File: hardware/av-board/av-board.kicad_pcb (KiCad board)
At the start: 4 copper layers, 94.6 x 69.4 mm, 222 parts, among them J1 RCA Y, J10 2x20 socket, J2 RCA Pb, J3 RCA Pr, J4 RCA L, J5 RCA R, J6 HDMI-001, J9 2x20 socket, SW1 TS-1187A-B-A-B, SW2 TS-1187A-B-A-B, U1 ADV7842KBCZ-5, U10 TPD4E05U06DQAR, U2 ADV7511KSTZ, U3 PCM1808PWR, U4 TLV62569DBVR, U5 TPS7A7001DDAR, U6 TPS7A7001DDAR, U7 TPS7A7001DDAR, U8 TPD4E05U06DQAR, U9 TPD4E05U06DQAR, Y1 28.63636MHz 20pF

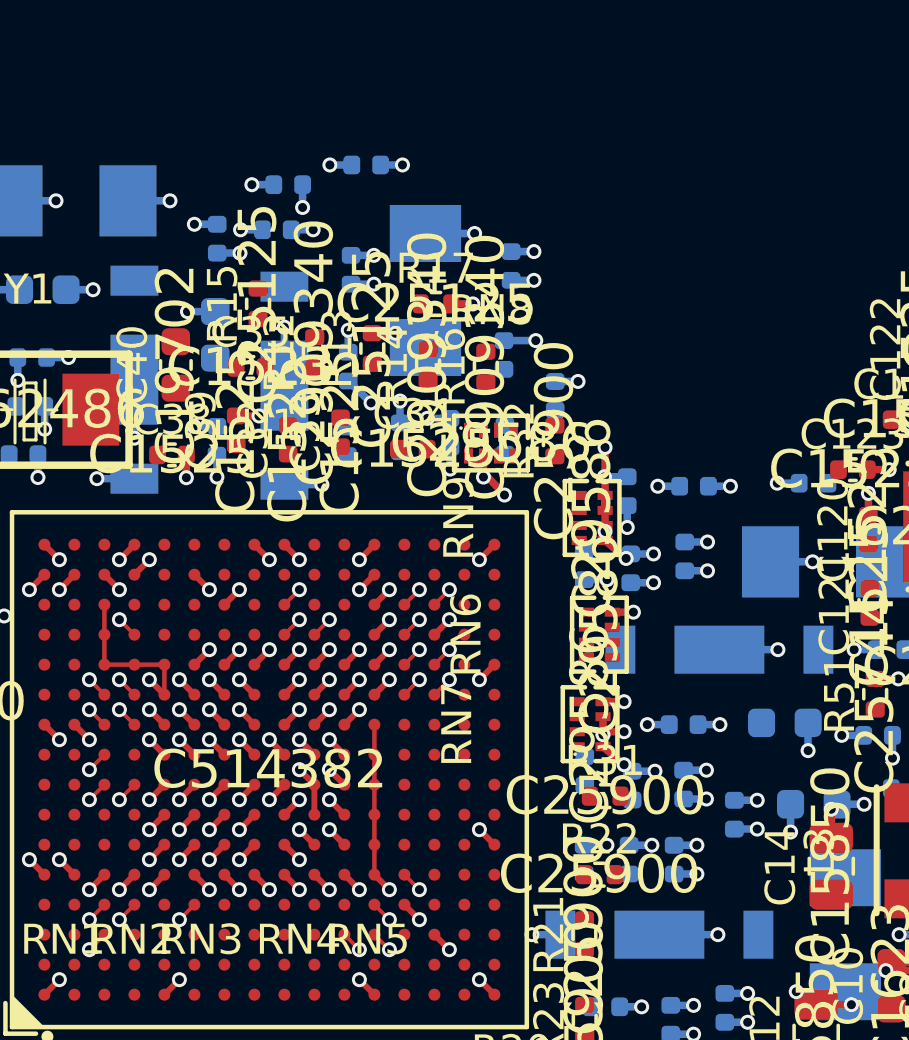
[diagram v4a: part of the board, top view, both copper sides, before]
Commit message: SDRAM pull-downs grouped by ball position, arrays along the BGA's right side; six layers default
The pull-down arrays were grouped by DQ number, so each collected four lines from scattered
balls across the BGA's top right corner (RN8: R16, R15, T15 and N14, four rows in), and lines
for different arrays crossed in the tightest spot on the board. Any pin may take any of these
identical 4.7 k pull-downs, so:

- board.py orders the 18 balls along the chip's T-row edge (column, then row); each array serves
  four neighbouring balls, the two at the ends of the run take single resistors.
- gen_pcb.py's array placer (was place_rn, for the 75 R arrays) takes any side: the pull-down
  arrays now stand in a column down the ADV7842's right side, each level with its balls, pads
  towards the chip in ball order.
- Six layers are the default (LAYERS=4 does not route); design.md says why, with the results.

ERC clean, schematic = board.py (903 pins), DRC: only the unrouted connections.

Co-Authored-By: Claude Opus 5.5 <noreply@anthropic.com>
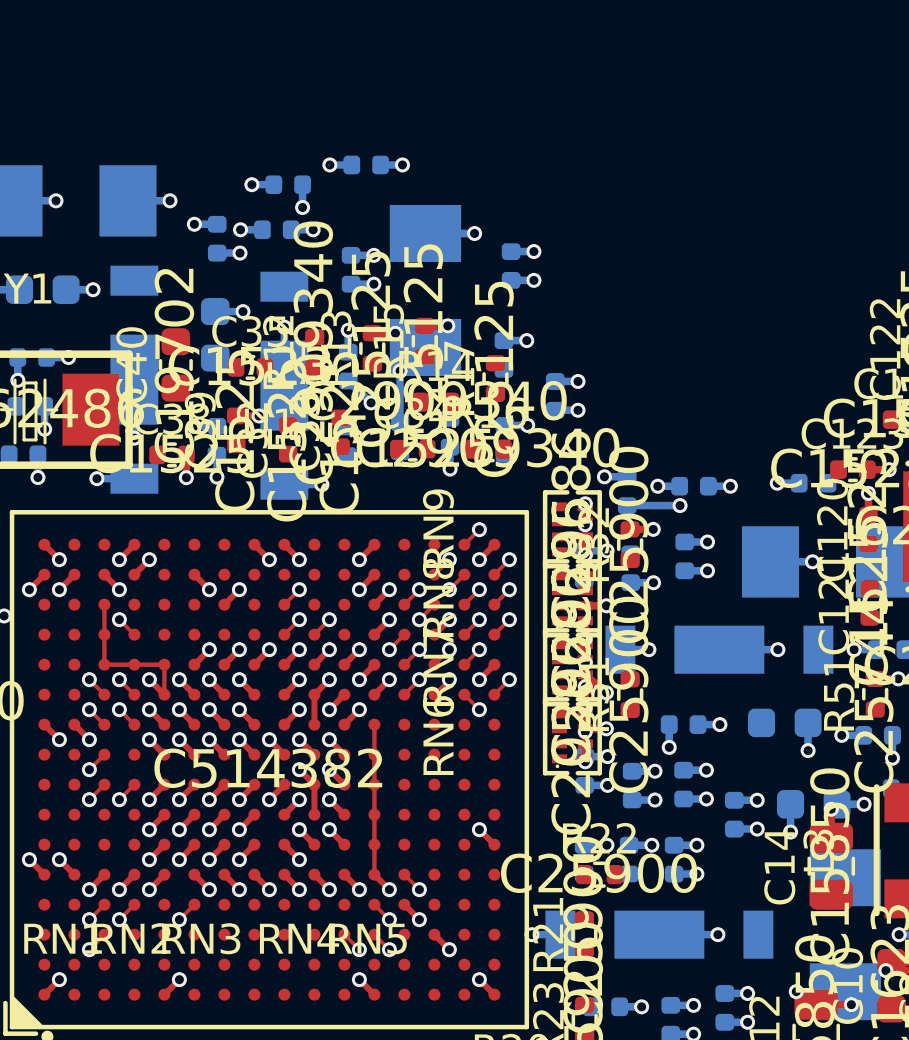
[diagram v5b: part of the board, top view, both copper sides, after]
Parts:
- moved RN8 5.84 mm to (123.1, 55.3), turned to 90 degrees
- moved R15 5.69 mm to (118.2, 46.7)
- moved R32 4.27 mm to (125.0, 53.5)
- moved RN6 3.51 mm to (123.1, 59.9)
- moved R31 3.48 mm to (125.0, 58.5), turned to 90 degrees
- moved R17 3.18 mm to (120.5, 48.0), turned to 90 degrees
- moved R16 2.74 mm to (120.3, 50.3), turned to 0 degrees
- moved RN7 1.99 mm to (123.1, 57.6)
- moved R14 1.28 mm to (118.5, 48.7), turned to 0 degrees
- moved RN9 0.76 mm to (123.1, 53.0)
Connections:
- R32 pad 1: PD_SDRAM_UDQS -> PD_SDRAM_DQ8
- RN6 pad 1: PD_SDRAM_DQ0 -> PD_SDRAM_DQ7
- RN6 pad 2: PD_SDRAM_DQ1 -> PD_SDRAM_DQ6
- RN6 pad 3: PD_SDRAM_DQ2 -> PD_SDRAM_DQ5
- RN6 pad 4: PD_SDRAM_DQ3 -> PD_SDRAM_DQ4
- RN7 pad 1: PD_SDRAM_DQ4 -> PD_SDRAM_DQ3
- RN7 pad 2: PD_SDRAM_DQ5 -> PD_SDRAM_DQ2
- RN7 pad 3: PD_SDRAM_DQ6 -> PD_SDRAM_DQ15
- RN7 pad 4: PD_SDRAM_DQ7 -> PD_SDRAM_DQ0
- RN8 pad 1: PD_SDRAM_DQ8 -> PD_SDRAM_DQ1
- RN8 pad 2: PD_SDRAM_DQ9 -> PD_SDRAM_DQ11
- RN8 pad 3: PD_SDRAM_DQ10 -> PD_SDRAM_DQ12
- RN8 pad 4: PD_SDRAM_DQ11 -> PD_SDRAM_DQ13
- RN9 pad 1: PD_SDRAM_DQ12 -> PD_SDRAM_DQ14
- RN9 pad 2: PD_SDRAM_DQ13 -> PD_SDRAM_UDQS
- RN9 pad 3: PD_SDRAM_DQ14 -> PD_SDRAM_DQ9
- RN9 pad 4: PD_SDRAM_DQ15 -> PD_SDRAM_DQ10
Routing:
- net AV_DVDDIO: track 20.8 -> 22.3 mm, vias 21 -> 23
- net AV_VDD: track 11.9 -> 13.1 mm
- net AV_AVDD: track 14.1 -> 14.9 mm, vias 17 -> 18
- net PD_SDRAM_UDQS: track 0.00 -> 0.71 mm, vias 0 -> 1
- net PD_SDRAM_DQ9: track 0.00 -> 0.71 mm, vias 0 -> 1
- net PD_SDRAM_DQ8: track 0.00 -> 0.71 mm, vias 0 -> 1
- net PD_SDRAM_DQ6: track 0.00 -> 0.71 mm, vias 0 -> 1
- net PD_SDRAM_DQ5: track 0.00 -> 0.71 mm, vias 0 -> 1
- net PD_SDRAM_DQ2: track 0.00 -> 0.71 mm, vias 0 -> 1
- net PD_SDRAM_DQ14: track 0.00 -> 0.71 mm, vias 0 -> 1
- net PD_SDRAM_DQ13: track 0.00 -> 0.71 mm, vias 0 -> 1
- net PD_SDRAM_DQ10: track 0.00 -> 0.71 mm, vias 0 -> 1
- net PD_SDRAM_DQ1: track 0.00 -> 0.71 mm, vias 0 -> 1
- net PD_SDRAM_DQ0: track 0.00 -> 0.71 mm, vias 0 -> 1
- net GND: track 249.6 -> 249.8 mm, vias 270 -> 273
- added copper zone on In3.Cu, net AV_AVDD
- added copper zone on In3.Cu, net AV_DVDDIO
- added copper zone on In3.Cu, net AV_PVDD
- added copper zone on In3.Cu, net AV_TVDD
- added copper zone on In3.Cu, net AV_VDD
- added copper zone on In4.Cu, net GND
- removed copper zone on In2.Cu, net AV_AVDD
- removed copper zone on In2.Cu, net AV_DVDDIO
- removed copper zone on In2.Cu, net AV_PVDD
- removed copper zone on In2.Cu, net AV_TVDD
- removed copper zone on In2.Cu, net AV_VDD
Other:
- copper layers 4 -> 6

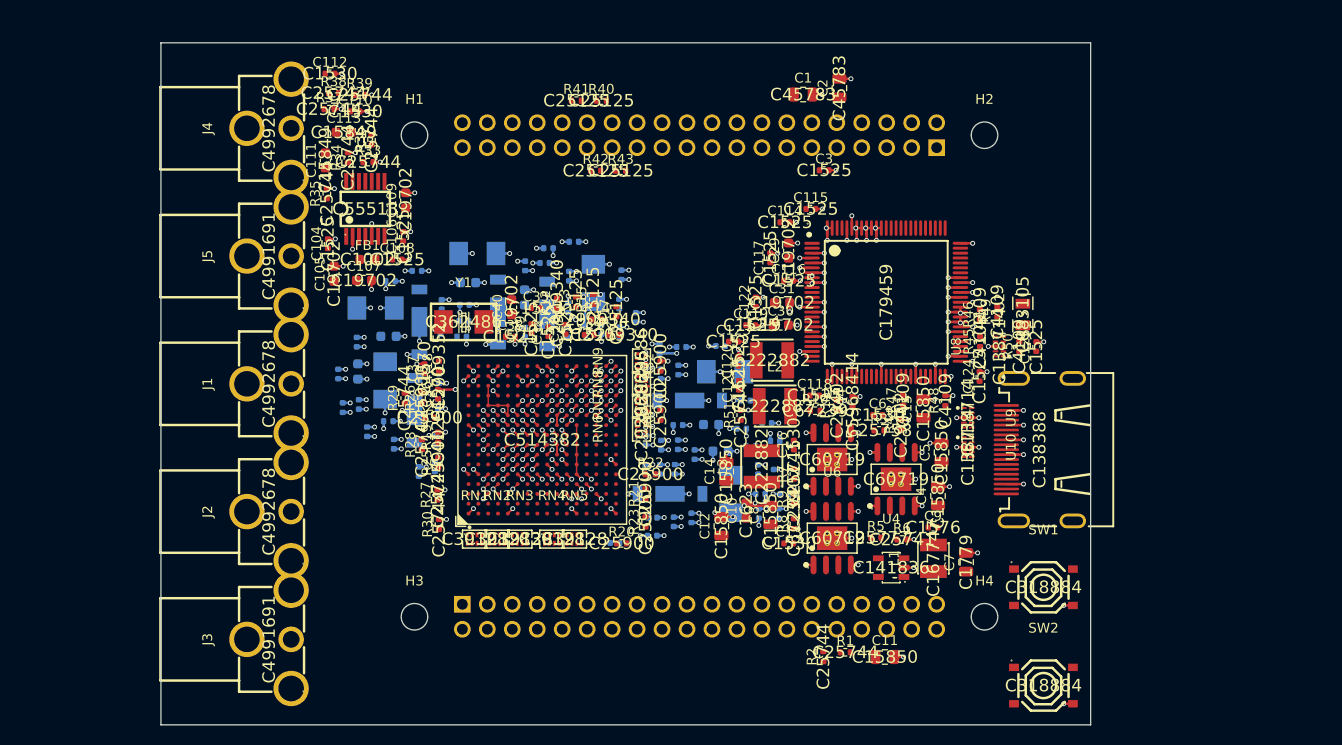
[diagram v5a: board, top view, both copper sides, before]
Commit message: Single pull-down resistors, SYNC_Y escape via, rail caps by their rail pad
From a round of free Freerouting trials (each variant routed on fpga, DRC'd, failures counted
over several runs):

- The unused SDRAM port's 18 pull-downs are single 0402s by the ADV7842's right side. With
  4-resistor arrays two to five of them failed in every run on both routers (four lines meeting a
  0.5 mm-pitch array in order, in the board's tightest corner); with singles, rarely one.
- SYNC_Y (J15) takes an escape via like the pull-down balls: it failed in nearly every run on
  F.Cu under the analog inputs' terminations, and not once with the via.
- A rail cap is placed where its rail pad (0.3 mm in) is over its plane, not its whole footprint:
  all 69 now sit on their planes (three were off). The plane fanout puts a rail pad's via only
  where the via itself lands on the plane (one off it connected nothing), tries 16 directions up
  to 2.5 mm, and names the pads left without one (their caps are joined by a routed track).
- CVDD's filter FL3 sits beside FL6, a short branch off FL4's 1V8A.

Tried and dropped: a wider free ring above the analog edge, more room round each rail cap,
reserved via spots, pull-down arrays on B.Cu or further out, vias for REFP/REFN, turning U5/U7.

Freerouting on this board leaves 2-7 short connections depending on the run. ERC clean,
schematic = board.py, DRC: only the unrouted connections.

Co-Authored-By: Claude Opus 5.5 <noreply@anthropic.com>
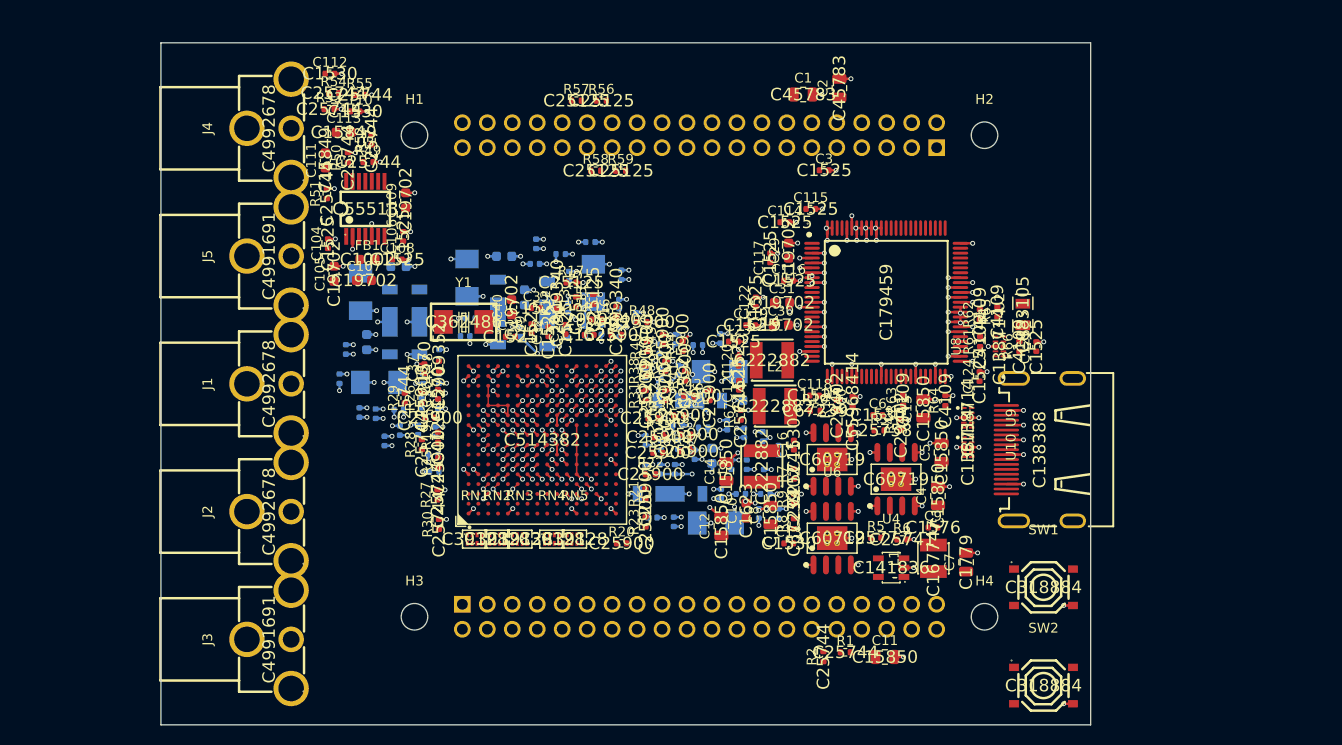
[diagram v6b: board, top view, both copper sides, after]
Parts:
- removed RN6, RN7, RN8, RN9: 4.7k, lcsc:RES-ARRAY-SMD_0402-8P-L2.0-W1.0-BL
- added R52: 10k, Resistor_SMD:R_0402_1005Metric, F.Cu at (95.6, 30.5)
- added R53: 10k, Resistor_SMD:R_0402_1005Metric, F.Cu at (91.3, 27.3)
- added R54: 10k, Resistor_SMD:R_0402_1005Metric, F.Cu at (91.8, 25.7)
- added R55: 10k, Resistor_SMD:R_0402_1005Metric, F.Cu at (94.4, 25.9)
- added R56: 51, Resistor_SMD:R_0402_1005Metric, F.Cu at (119.0, 26.5)
- added R57: 51, Resistor_SMD:R_0402_1005Metric, F.Cu at (116.5, 26.5)
- added R58: 51, Resistor_SMD:R_0402_1005Metric, F.Cu at (118.4, 33.6)
- added R59: 51, Resistor_SMD:R_0402_1005Metric, F.Cu at (121.0, 33.6)
- added R60: 887, Resistor_SMD:R_0402_1005Metric, F.Cu at (144.6, 57.1)
- added R61: 2k, Resistor_SMD:R_0402_1005Metric, F.Cu at (157.6, 51.0)
- added R62: 2k, Resistor_SMD:R_0402_1005Metric, F.Cu at (157.5, 48.2)
- added R63: 2k, Resistor_SMD:R_0402_1005Metric, F.Cu at (149.7, 57.0)
- added R64: 2k, Resistor_SMD:R_0402_1005Metric, F.Cu at (154.0, 57.0)
- added R65: 2k, Resistor_SMD:R_0402_1005Metric, F.Cu at (159.3, 48.0)
- added R66: 2k, Resistor_SMD:R_0402_1005Metric, F.Cu at (161.6, 51.5)
- added R67: 10k, Resistor_SMD:R_0402_1005Metric, F.Cu at (133.2, 58.5)
- R33, R34, R35, R36, R37, R38, R39: value 10k -> 4.7k
- R40, R41, R42, R43: value 51 -> 4.7k
- R44: value 887 -> 4.7k
- R45, R46, R47, R48: value 2k -> 4.7k
- R49, R50: value 2k -> 10k
- moved R50 71.0 mm to (93.2, 32.3)
- moved R49 65.8 mm to (95.3, 32.7), turned to 0 degrees
- moved R37 49.1 mm to (127.6, 60.5)
- moved R51 47.8 mm to (91.1, 36.0)
- moved R36 43.1 mm to (124.8, 62.3), turned to 0 degrees
- moved R34 42.7 mm to (126.9, 58.5), turned to 0 degrees
- moved R38 42.5 mm to (123.5, 54.0), turned to 90 degrees
- moved R35 41.9 mm to (124.9, 60.7), turned to 0 degrees
- moved R39 41.6 mm to (125.5, 53.5), turned to 90 degrees
- moved R33 39.0 mm to (124.3, 58.8)
- moved R45 37.0 mm to (120.5, 50.3), turned to 0 degrees
- moved R48 31.9 mm to (123.1, 49.0), turned to 0 degrees
- moved R41 30.1 mm to (127.5, 54.5), turned to 90 degrees
- moved R46 28.7 mm to (130.0, 56.5)
- moved R40 25.4 mm to (123.7, 51.5), turned to 90 degrees
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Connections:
- R31 pad 1: PD_SDRAM_LDQS -> PD_SDRAM_DQ0
- R32 pad 1: PD_SDRAM_DQ8 -> PD_SDRAM_DQ1
- R33 pad 1: MD0 -> PD_SDRAM_DQ2
- R34 pad 1: MD1 -> PD_SDRAM_DQ3
- R35 pad 1: FMT -> PD_SDRAM_DQ4
- R36 pad 1: RCA_L -> PD_SDRAM_DQ5
- R36 pad 2: AUD_DIV_L -> GND
- R37 pad 1: AUD_DIV_L -> PD_SDRAM_DQ6
- R38 pad 1: RCA_R -> PD_SDRAM_DQ7
- R38 pad 2: AUD_DIV_R -> GND
- R39 pad 1: AUD_DIV_R -> PD_SDRAM_DQ8
- R40 pad 1: OUT_MCLK -> PD_SDRAM_DQ9
- R40 pad 2: TX_MCLK -> GND
- R41 pad 1: OUT_SCLK -> PD_SDRAM_DQ10
- R41 pad 2: TX_SCLK -> GND
- R42 pad 1: OUT_LRCLK -> PD_SDRAM_DQ11
- R42 pad 2: TX_LRCLK -> GND
- R43 pad 1: OUT_I2S0 -> PD_SDRAM_DQ12
- R43 pad 2: TX_I2S0 -> GND
- R44 pad 1: R_EXT -> PD_SDRAM_DQ13
- R45 pad 1: 3V3 -> PD_SDRAM_DQ14
- R45 pad 2: OUT_SCL -> GND
- R46 pad 1: 3V3 -> PD_SDRAM_DQ15
- R46 pad 2: OUT_SDA -> GND
- R47 pad 1: 3V3 -> PD_SDRAM_LDQS
- R47 pad 2: OUT_INT -> GND
- R48 pad 1: OUT_PD -> PD_SDRAM_UDQS
- R49 pad 1: HDMI_5V -> MD0
- R49 pad 2: HDMI_SCL -> GND
- R50 pad 1: HDMI_5V -> MD1
- R50 pad 2: HDMI_SDA -> GND
- R51 pad 1: HDMI_HPD -> FMT
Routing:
- net AV_DVDDIO: track 22.3 -> 27.3 mm, vias 23 -> 25
- net AV_VDD: track 13.1 -> 16.8 mm, vias 15 -> 17
- net GND: track 249.8 -> 246.8 mm, vias 273 -> 268
- net AV_TVDD: track 14.7 -> 15.5 mm, vias 18 -> 19
- net SYNC_Y: track 0.00 -> 0.71 mm, vias 0 -> 1
- net AV_AVDD: track 14.9 -> 15.1 mm, vias 18 -> 16

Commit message: The AV board routed: six layers, DRC clean
av-board.kicad_pcb is now routed: Freerouting 1.9 (60 passes) on the six-layer placement, then
mazeroute.py for the two connections it left (C20's AVDD pad round C54, and the Y5 pixel line
from U1 L2 to RN5). DRC: no unconnected items, no clearance or short violations, nothing
dangling; only silkscreen warnings and the two sockets' renumbered pads.

mazeroute.py is a small grid router (A*) for what an autorouter leaves: one net between two
pads on F.Cu/In2.Cu/B.Cu, round everything on the board with our clearances, a new via where
one fits on all layers with drill spacing; obstacles dumped by KiCad's python, the search in
numpy (eda-venv), the result applied back and the zones refilled. Paths start and end at pad
centres.

Checked after routing (design.md "Routing"): nothing switching near R_EXT; TMDS intra-pair skew
at most 2.4 mm, but Freerouting routes the pairs' halves apart, through vias: laying the four
pairs in by hand, coupled and matched, is the next step.

Co-Authored-By: Claude Opus 5.5 <noreply@anthropic.com>
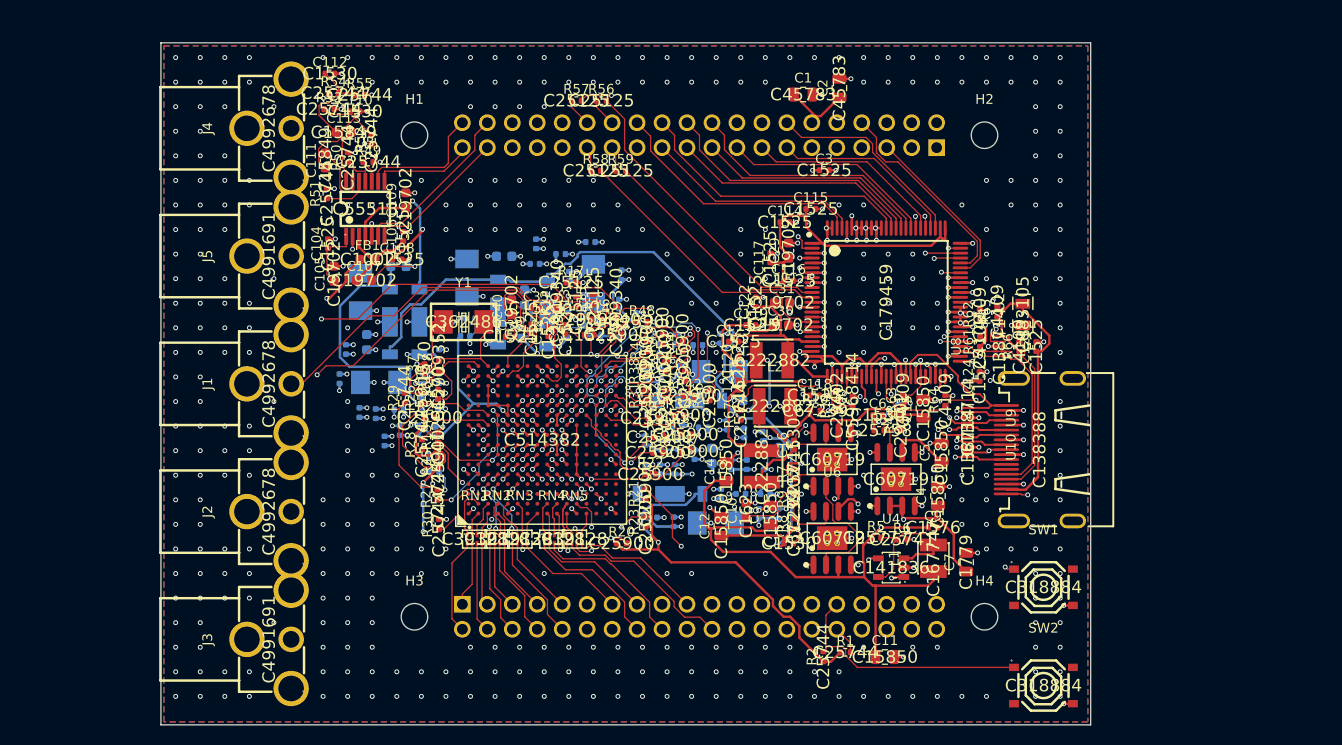
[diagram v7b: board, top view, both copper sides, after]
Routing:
- net 3V3: track 0.00 -> 219.7 mm, vias 0 -> 11
- net +5V: track 1.41 -> 197.6 mm, vias 2 -> 8
- net 1V8A: track 0.00 -> 95.3 mm, vias 0 -> 2
- net AIN_Y: track 0.71 -> 78.3 mm, vias 1 -> 2
- net 2V5: track 0.00 -> 75.1 mm, vias 0 -> 3
- net TX_DVDD: track 0.00 -> 66.8 mm, vias 0 -> 4
- net RCA_PR: track 0.00 -> 59.3 mm, vias 0 -> 2
- net HDMI_HPD: track 0.00 -> 58.4 mm, vias 0 -> 5
- net RCA_PB: track 0.00 -> 55.8 mm, vias 0 -> 1
- net TX_AVDD: track 0.00 -> 49.6 mm, vias 0 -> 3
- net GND: track 246.8 -> 295.8 mm, vias 268 -> 646
- net AV_CVDD: track 5.71 -> 53.2 mm
- net OUT_PD: track 0.00 -> 45.5 mm, vias 0 -> 1
- net TX_SCLK: track 0.00 -> 43.4 mm, vias 0 -> 2
- net 1V8B: track 0.00 -> 36.9 mm, vias 0 -> 2
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- added copper zone on B.Cu, net GND
- added copper zone on F.Cu, net GND
